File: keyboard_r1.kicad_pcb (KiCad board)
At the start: 2 copper layers, 155 parts, among them SW1 MX_SW_solder, SW10 MX_SW_solder, SW11 MX_SW_solder, SW12 MX_SW_solder, SW13 MX_SW_solder, SW14 MX_SW_solder, SW15 MX_SW_solder, SW16 MX_SW_solder, SW17 MX_SW_solder, SW18 MX_SW_solder, SW19 MX_SW_solder, SW2 MX_SW_solder, SW20 MX_SW_solder, SW21 MX_SW_solder, SW22 MX_SW_solder, SW23 MX_SW_solder, SW24 MX_SW_solder, SW25 MX_SW_solder, SW26 MX_SW_solder, SW27 MX_SW_solder, SW28 MX_SW_solder, SW29 MX_SW_solder, SW3 MX_SW_solder, SW30 MX_SW_solder, SW31 MX_SW_solder, SW32 MX_SW_solder, SW33 MX_SW_solder, SW34 MX_SW_solder, SW35 MX_SW_solder, SW36 MX_SW_solder, SW37 MX_SW_solder, SW38 MX_SW_solder, SW39 MX_SW_solder, SW4 MX_SW_solder, SW40 MX_SW_solder, SW41 MX_SW_solder, SW42 MX_SW_solder, SW43 MX_SW_solder, SW44 MX_SW_solder, SW45 MX_SW_solder, SW46 MX_SW_solder, SW47 MX_SW_solder, SW48 MX_SW_solder, SW49 MX_SW_solder, SW5 MX_SW_solder, SW50 MX_SW_solder, SW51 MX_SW_solder, SW52 MX_SW_solder, SW53 MX_SW_solder, SW54 MX_SW_solder, SW55 MX_SW_solder, SW56 MX_SW_solder, SW57 MX_SW_solder, SW58 MX_SW_solder, SW59 MX_SW_solder, SW6 MX_SW_solder, SW60 MX_SW_solder, SW61 MX_SW_solder, SW62 MX_SW_solder, SW63 MX_SW_solder, SW64 MX_SW_solder, SW65 MX_SW_solder, SW66 MX_SW_solder, SW67 MX_SW_solder, SW68 MX_SW_solder, SW69 MX_SW_solder, SW7 MX_SW_solder, SW70 MX_SW_solder, SW71 MX_SW_solder, SW72 MX_SW_solder, SW73 MX_SW_solder, SW74 MX_SW_solder, SW75 MX_SW_solder, SW76 MX_SW_solder, SW8 MX_SW_solder, SW9 MX_SW_solder

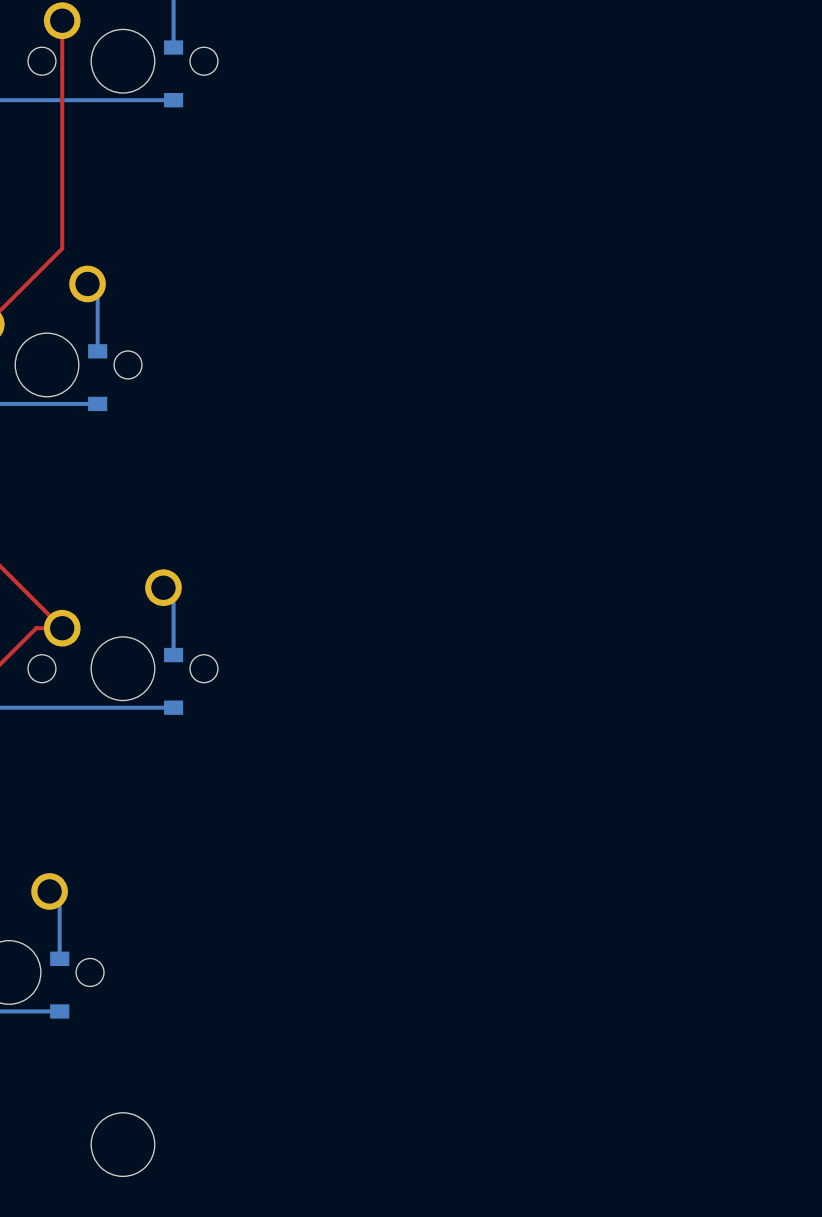
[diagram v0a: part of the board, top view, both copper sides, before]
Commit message: added Raspberry Pi Pico componenet
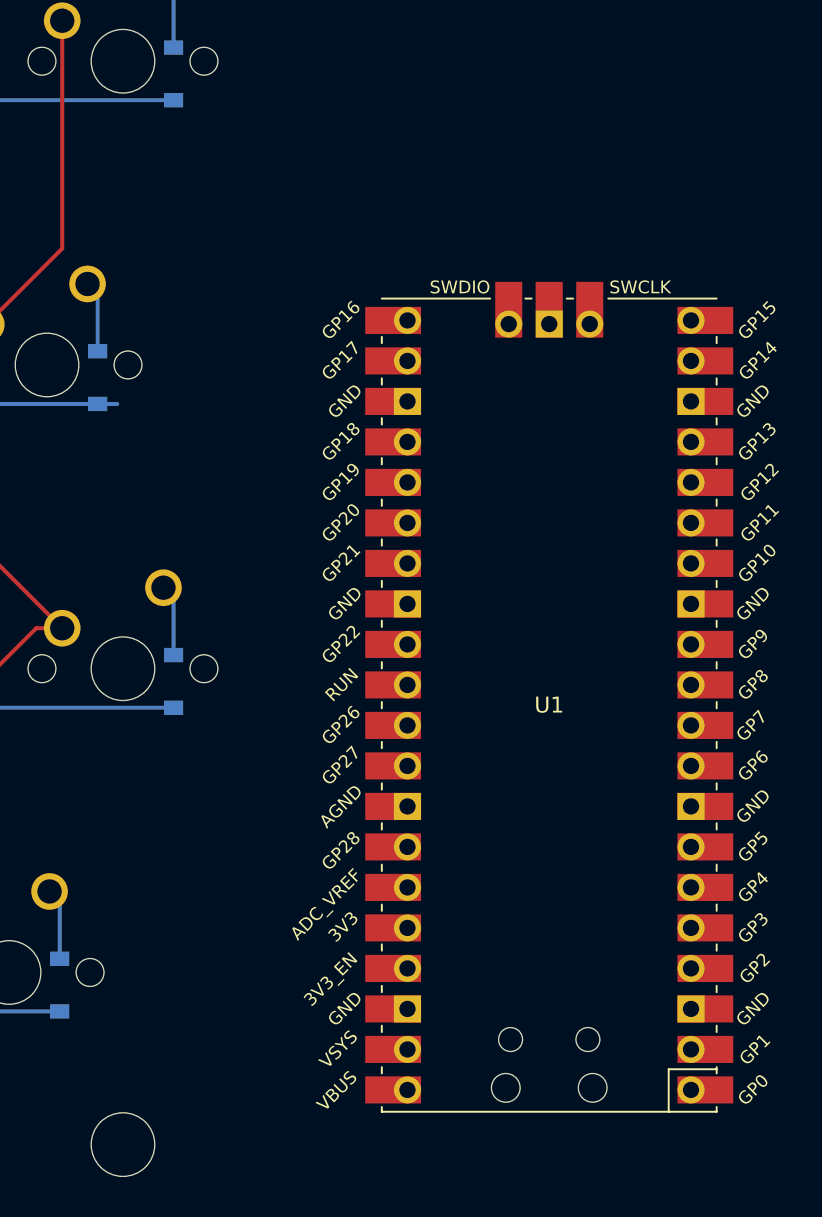
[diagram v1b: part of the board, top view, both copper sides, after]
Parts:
- added U1: Pico, MCU_RaspberryPi_and_Boards:RPi_Pico_SMD_TH, F.Cu at (361.7, 135.6)
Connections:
- net Net-(D10-Pad1) renamed ROW0
- net Net-(D25-Pad1) renamed ROW1
- net Net-(D60-Pad1) renamed ROW3
- net Net-(D72-Pad1) renamed ROW4
- net Net-(SW1-Pad1) renamed COL0
- net Net-(SW16-Pad1) renamed COL1
- net Net-(SW17-Pad1) renamed COL2
- net Net-(SW18-Pad1) renamed COL3
- net Net-(SW20-Pad1) renamed COL5
- net Net-(SW24-Pad1) renamed COL9
- net Net-(SW35-Pad1) renamed COL6
- net Net-(SW36-Pad1) renamed COL7
- net Net-(SW39-Pad1) renamed COL10
- net Net-(SW40-Pad1) renamed COL11
- net Net-(SW41-Pad1) renamed COL12
- net Net-(SW42-Pad1) renamed COL13
- net Net-(SW5-Pad1) renamed COL4
- net Net-(SW9-Pad1) renamed COL8
- D29 pad 1: Net-(D35-Pad1) -> ROW2
- D30 pad 1: Net-(D35-Pad1) -> ROW2
- D31 pad 1: Net-(D35-Pad1) -> ROW2
- D32 pad 1: Net-(D35-Pad1) -> ROW2
- D33 pad 1: Net-(D35-Pad1) -> ROW2
- D34 pad 1: Net-(D35-Pad1) -> ROW2
- D35 pad 1: Net-(D35-Pad1) -> ROW2
- D36 pad 1: Net-(D35-Pad1) -> ROW2
- D37 pad 1: Net-(D35-Pad1) -> ROW2
- D38 pad 1: Net-(D35-Pad1) -> ROW2
- D39 pad 1: Net-(D35-Pad1) -> ROW2
- D40 pad 1: Net-(D35-Pad1) -> ROW2
- D41 pad 1: Net-(D35-Pad1) -> ROW2
- D42 pad 1: Net-(D35-Pad1) -> ROW2
- D43 pad 1: Net-(D47-Pad1) -> ROW2
- D44 pad 1: Net-(D47-Pad1) -> ROW2
- D45 pad 1: Net-(D47-Pad1) -> ROW2
- D46 pad 1: Net-(D47-Pad1) -> ROW2
- D47 pad 1: Net-(D47-Pad1) -> ROW2
- D48 pad 1: Net-(D47-Pad1) -> ROW2
- D49 pad 1: Net-(D47-Pad1) -> ROW2
- D50 pad 1: Net-(D47-Pad1) -> ROW2
- D51 pad 1: Net-(D47-Pad1) -> ROW2
- D52 pad 1: Net-(D47-Pad1) -> ROW2
- D53 pad 1: Net-(D47-Pad1) -> ROW2
- D54 pad 1: Net-(D47-Pad1) -> ROW2
- D55 pad 1: Net-(D47-Pad1) -> ROW2
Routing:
- net ROW2: track 0.00 -> 495.4 mm
- net Net-(D35-Pad1): track 252.4 -> 0.00 mm
- net Net-(D47-Pad1): track 242.9 -> 0.00 mm
- net ROW1: track 252.4 -> 253.6 mm

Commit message: added all global labels
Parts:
- turned U1 to 0 degrees
